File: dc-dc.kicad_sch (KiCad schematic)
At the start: 130 parts, among them SW3 CVS-02B, U30 NCP718ASN500T1G, U31 MPM54304GMN, U32 MPM54304GMN, U33 MAX16150AUT+T, U34 NCP451AFCT2G, U35 SN74LVC1G125DBVR, U36 LM3880, U37 MP8869S, U38 TPS7A20185PDQNR, U39 NCP51400MNTXG, U40 XC6230H001ER-G, U41 REF3012AIDBZT

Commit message: Finish connecting MCU
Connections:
- net SEQ_EN: now reaches C339.1, R308.1, U36.3 (EN)
- net ~{PB_CTRL_CLR} renamed SUP_MCU.SW_STATE
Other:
- note added: "NOTE2: when Res to GND mounted -> Alawys ON mount sequencer EN cap"
- note added: "NOTE: mount 1/2"
- note added: "NOTE: populate when Always ON (see NOTE2)"
- note added: "Todo: POE_DC signal is not connected Change 5V_AON to 3.3V_AON"
- note removed: "DNP for always ON"
- note removed: "Mount 1/2"
- note removed: "Mount only for Always-ON"
- note removed: "Todo: POE_DC signal is not connected"
- moved on the sheet: C336, C337, C339, D33, R283, R284, R293, R294, R308, U33, U35

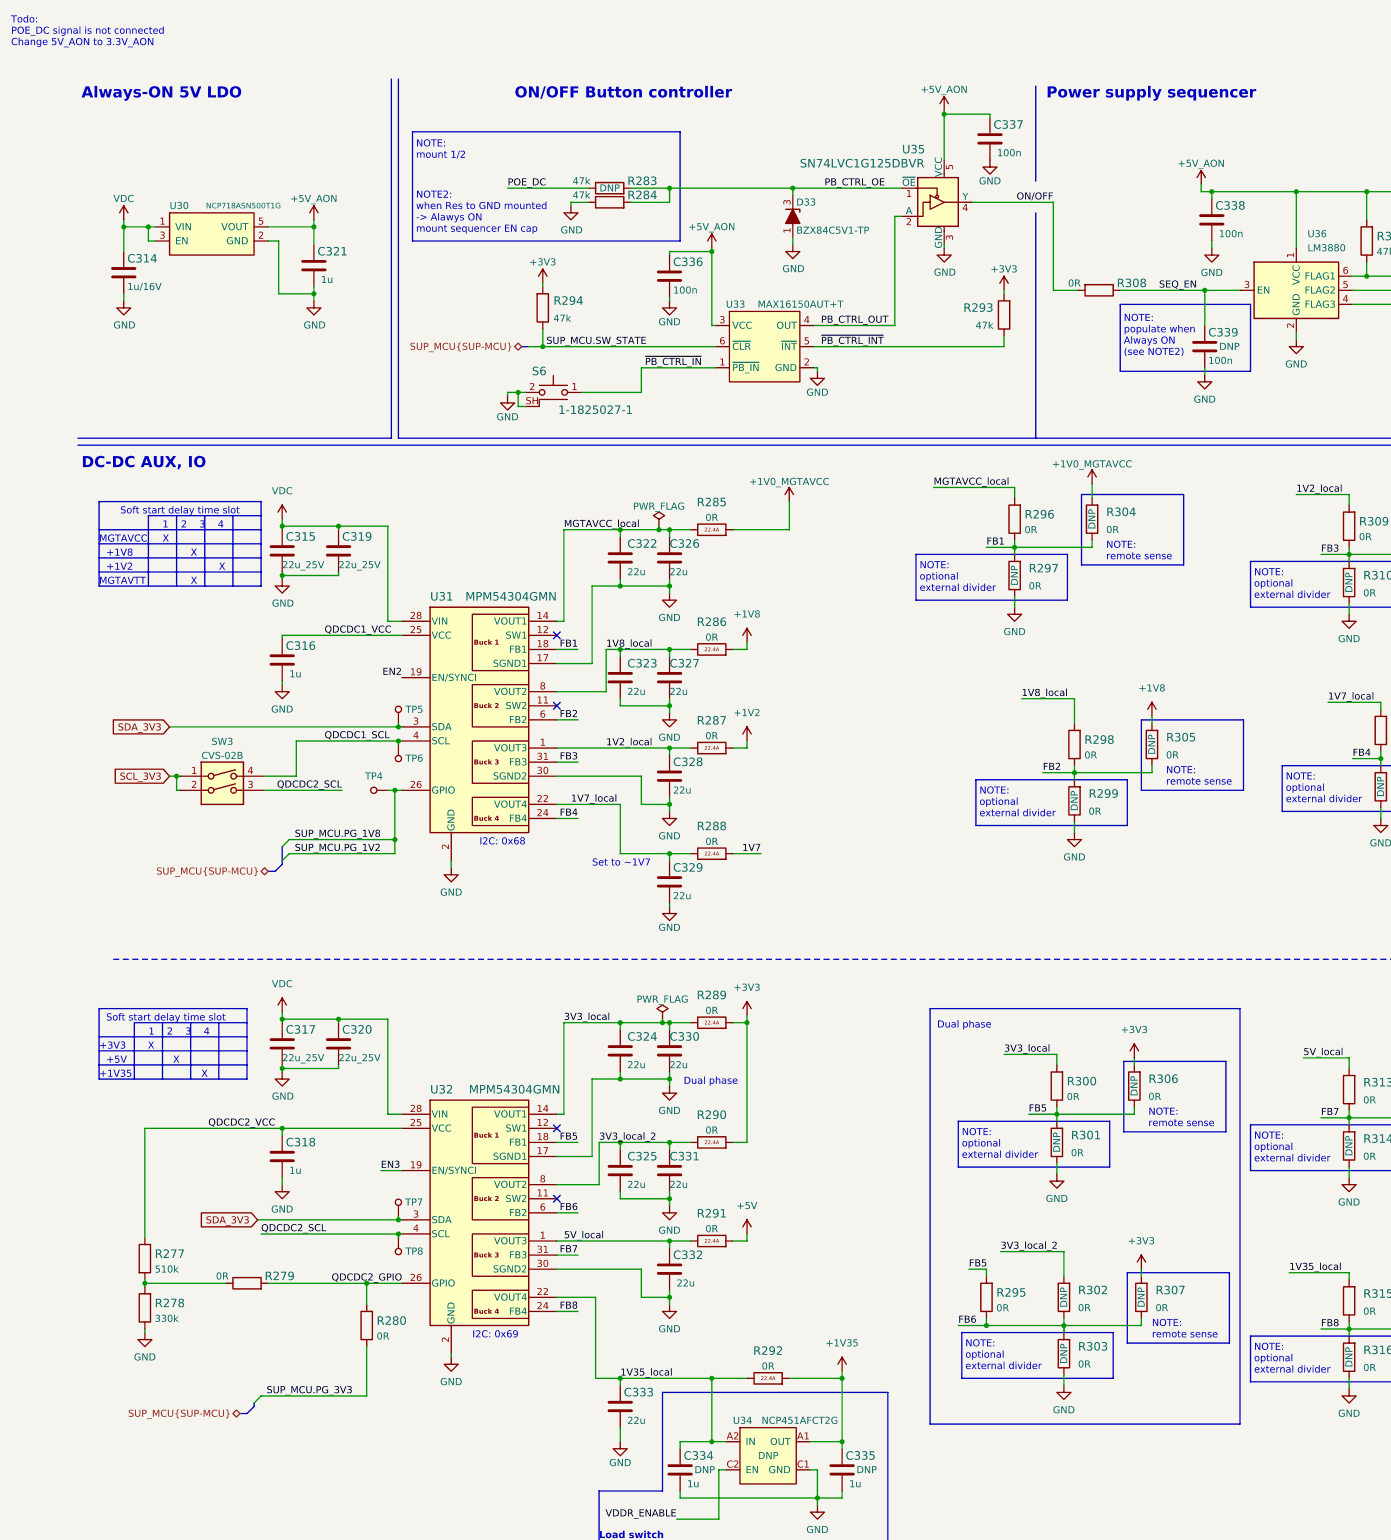
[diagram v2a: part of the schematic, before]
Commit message: DC-DC sheet grouping and placement on PCB
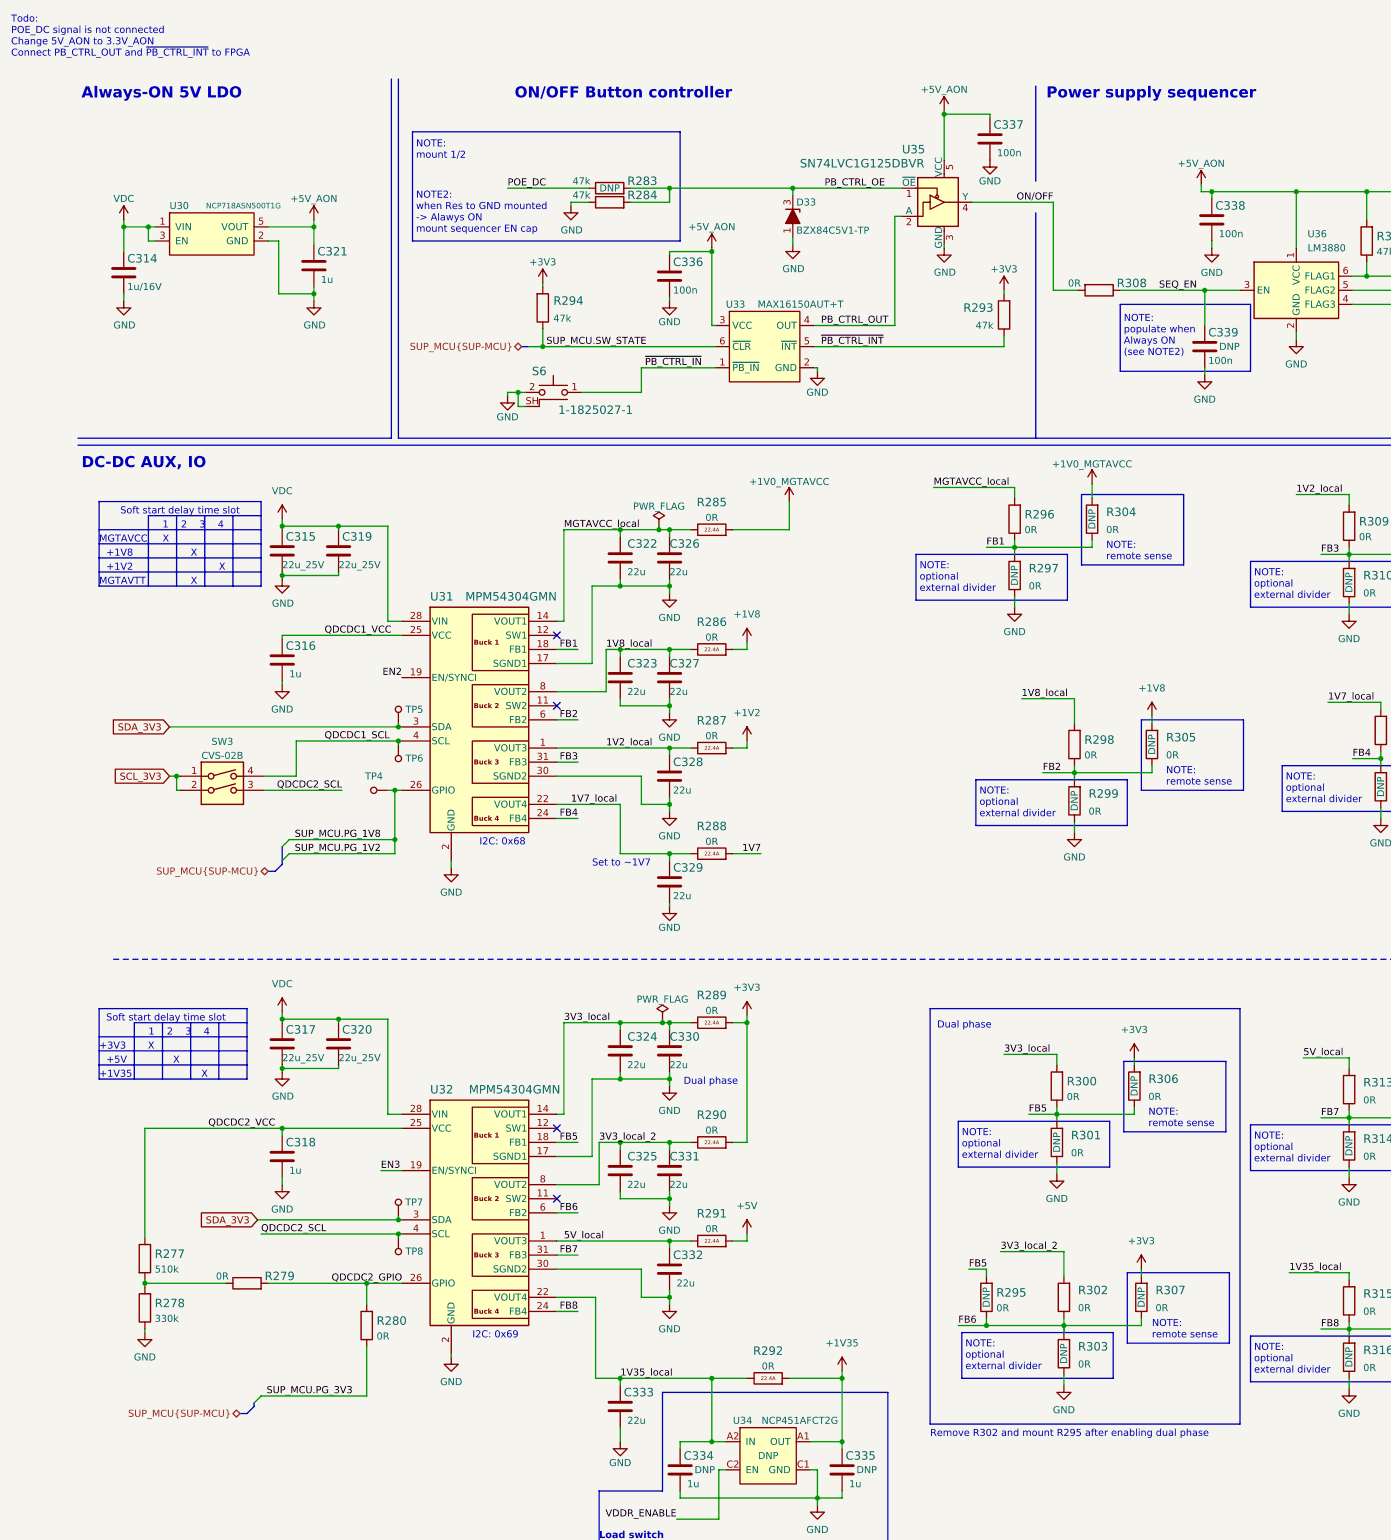
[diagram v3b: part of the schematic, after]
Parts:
- R295: DNP (none) -> DNP
- R302: DNP DNP -> (none)
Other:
- note added: "Remove R302 and mount R295 after enabling dual phase"
- note added: "Todo: POE_DC signal is not connected Change 5V_AON to 3.3V_AON Connect PB_CTRL_OUT and ~{PB_CTRL_INT} to FPGA"
- note removed: "Todo: POE_DC signal is not connected Change 5V_AON to 3.3V_AON"
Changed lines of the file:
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@@
     (effects (font (size 1.27 1.27)) (justify left bottom))
   )
-  (text "Todo:\nPOE_DC signal is not connected\nChange 5V_AON to 3.3V_AON"
-    (at 0.635 6.985 0)
+  (text "Todo:\nPOE_DC signal is not connected\nChange 5V_AON to 3.3V_AON\nConnect PB_CTRL_OUT and ~{PB_CTRL_INT} to FPGA"
+    (at 0.635 8.89 0)
     (effects (font (size 1.27 1.27)) (justify left bottom))
   )
@@
     (effects (font (size 2 2) (thickness 0.254) bold) (justify left bottom))
   )
+  (text "Remove R302 and mount R295 after enabling dual phase"
+    (at 166.37 257.81 0)
+    (effects (font (size 1.27 1.27)) (justify left bottom))
+  )
   (text "NOTE:\nmount 1/2" (at 73.66 27.305 0)
     (effects (font (size 1.27 1.27)) (justify left bottom))
@@
       (effects (font (size 1.27 1.27)) (justify right))
     )
-    (property "DNP" "DNP" (id 7) (at 190.5 232.41 0))
     (pin "1")
     (pin "2")
@@
   )
   (symbol (lib_id "antmicroResistors0402:R_0R_0402") (at 176.53 232.41 90) (unit 1)
-    (in_bom yes) (on_board yes) (fields_autoplaced)
+    (in_bom yes) (on_board yes)
     (property "Reference" "R295" (id 0) (at 178.308 231.5754 90)
       (effects (font (size 1.524 1.524)) (justify right))
@@
       (effects (font (size 1.27 1.27)) (justify right))
     )
+    (property "DNP" "DNP" (id 7) (at 176.53 232.41 0))
     (pin "1")
     (pin "2")

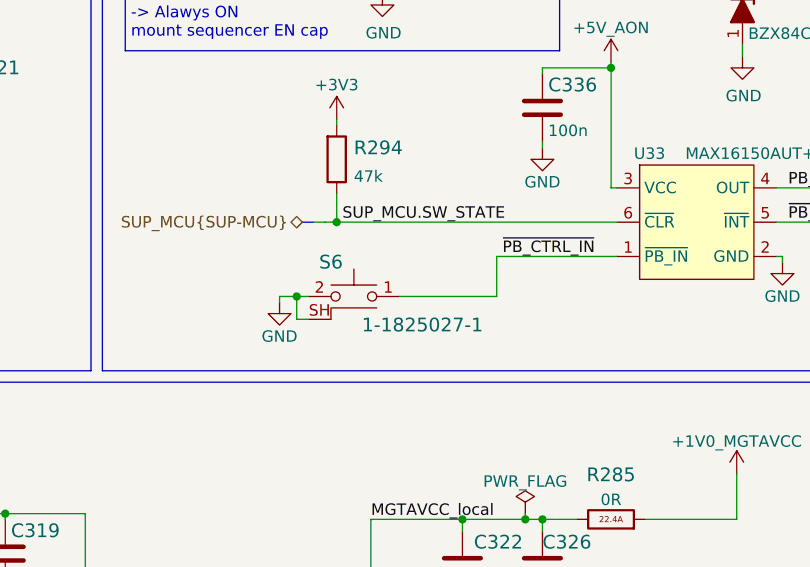
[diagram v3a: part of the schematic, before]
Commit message: Unify used buttons
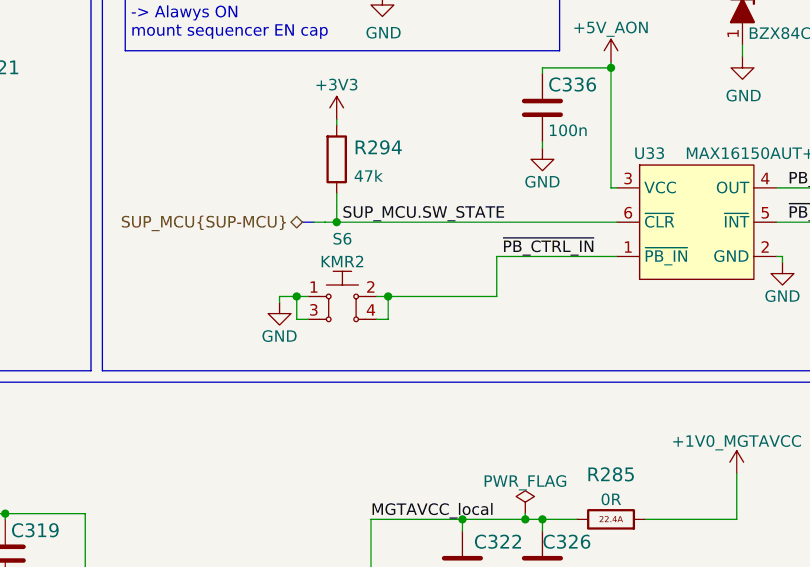
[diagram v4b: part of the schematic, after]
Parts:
- removed S6: 1-1825027-1, antmicro-footprints:TE_1-1825027-1, symbol antmicroTactileSwitches:1-1825027-1
- added S6: KMR2, antmicro-footprints:SW_SPST_4.2x2.8, symbol antmicroPushbuttonSwitches:KMR2
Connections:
- net GND: now also S6.1, S6.3
- net ~{PB_CTRL_IN}: now also S6.2, S6.4
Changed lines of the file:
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@@
   (junction (at 370.205 55.245) (diameter 0) (color 0 0 0 0)
   )
+  (junction (at 102.235 69.215) (diameter 0) (color 0 0 0 0)
+  )
   (junction (at 69.85 149.86) (diameter 0) (color 0 0 0 0)
   )
@@
     (stroke (width 0) (type default) (color 0 0 0 0))
   )
+  (wire (pts (xy 102.235 71.755) (xy 100.965 71.755))
+    (stroke (width 0) (type default) (color 0 0 0 0))
+  )
   (wire (pts (xy 192.405 137.795) (xy 206.375 137.795))
     (stroke (width 0) (type default) (color 0 0 0 0))
@@
     (stroke (width 0) (type default) (color 0 0 0 0))
   )
+  (wire (pts (xy 102.235 69.215) (xy 114.3 69.215))
+    (stroke (width 0) (type default) (color 0 0 0 0))
+  )
   (wire (pts (xy 379.095 45.085) (xy 379.095 46.355))
     (stroke (width 0) (type default) (color 0 0 0 0))
@@
     (stroke (width 0) (type default) (color 0 0 0 0))
   )
+  (wire (pts (xy 102.235 69.215) (xy 102.235 71.755))
+    (stroke (width 0) (type default) (color 0 0 0 0))
+  )
   (wire (pts (xy 206.375 127.635) (xy 206.375 128.905))
     (stroke (width 0) (type default) (color 0 0 0 0))
@@
     (stroke (width 0) (type default) (color 0 0 0 0))
   )
-  (wire (pts (xy 114.3 69.215) (xy 103.505 69.215))
+  (wire (pts (xy 100.965 69.215) (xy 102.235 69.215))
     (stroke (width 0) (type default) (color 0 0 0 0))
   )
@@
     (pin "2")
   )
+  (symbol (lib_id "antmicroPushbuttonSwitches:KMR2") (at 97.155 69.215 0) (unit 1)
+    (in_bom yes) (on_board yes) (fields_autoplaced)
+    (property "Reference" "S6" (id 0) (at 97.155 62.8482 0))
+    (property "Value" "KMR2" (id 1) (at 97.155 65.3851 0))
+    (property "Footprint" "antmicro-footprints:SW_SPST_4.2x2.8" (id 2) (at 102.235 64.135 0)
+      (effects (font (size 1.27 1.27)) (justify left) hide)
+    )
+    (property "Datasheet" "http://www.farnell.com/datasheets/2631211.pdf" (id 3) (at 102.235 61.595 0)
+      (effects (font (size 1.524 1.524)) (justify left) hide)
+    )
+    (property "MPN" "KMR211NGLFS" (id 4) (at 102.1334 59.2328 0)
+      (effects (font (size 1.524 1.524)) (justify left) hide)
+    )
+    (property "Manufacturer" "C&K Components" (id 5) (at 102.235 57.2262 0)
+      (effects (font (size 1.524 1.524)) (justify left) hide)
+    )
+    (pin "1")
+    (pin "2")
+    (pin "3")
+    (pin "4")
+  )
   (symbol (lib_id "antmicroCapacitors0402:C_10u_0402") (at 350.52 117.475 0) (unit 1)
     (in_bom yes) (on_board yes)
@@
     (pin "1")
   )
-  (symbol (lib_id "antmicroTactileSwitches:1-1825027-1") (at 98.425 67.945 0) (mirror y) (unit 1)
-    (in_bom yes) (on_board yes)
-    (property "Reference" "S6" (id 0) (at 95.885 65.405 0)
-      (effects (font (size 1.524 1.524)))
-    )
-    (property "Value" "1-1825027-1" (id 1) (at 106.045 72.39 0)
-      (effects (font (size 1.524 1.524)))
-    )
-    (property "Footprint" "antmicro-footprints:TE_1-1825027-1" (id 2) (at 93.345 62.865 0)
-      (effects (font (size 1.524 1.524)) (justify left) hide)
-    )
-    (property "Datasheet" "https://www.te.com/commerce/DocumentDelivery/DDEController?Action=showdoc&DocId=Customer+Drawing%7F1825027%7FH1%7Fpdf%7FEnglish%7FENG_CD_1825027_H1.pdf%7F1-1825027-1" (id 3) (at 93.345 60.325 0)
-      (effects (font (size 1.524 1.524)) (justify left) hide)
-    )
-    (property "MPN" "1-1825027-1" (id 4) (at 93.345 55.245 0)
-      (effects (font (size 1.524 1.524)) (justify left) hide)
-    )
-    (property "Manufacturer" "TE Connectivity" (id 5) (at 93.345 40.005 0)
-      (effects (font (size 1.524 1.524)) (justify left) hide)
-    )
-    (pin "1")
-    (pin "2")
-    (pin "SH")
-  )
   (symbol (lib_id "antmicroResistors0402:R_0R_0402") (at 189.23 194.31 90) (unit 1)

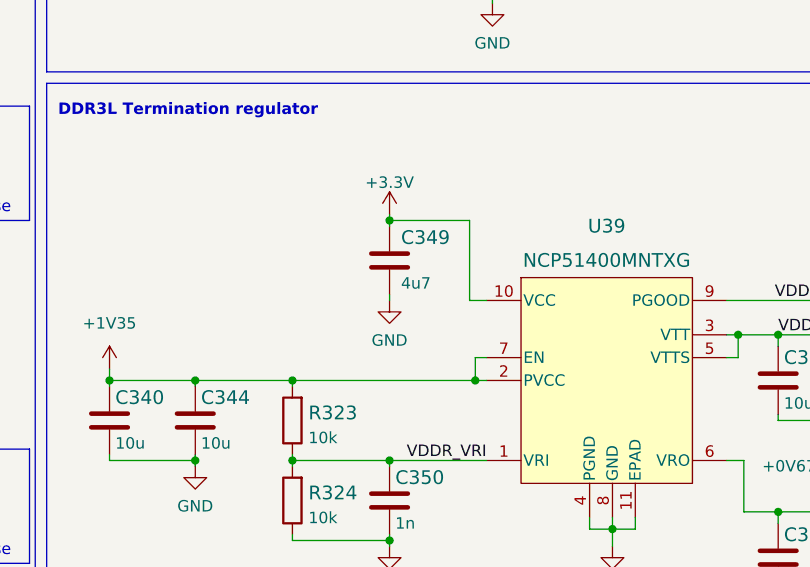
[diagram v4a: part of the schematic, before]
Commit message: Increase 0201 to 0402 components where possible (EIA 0402 footprint)
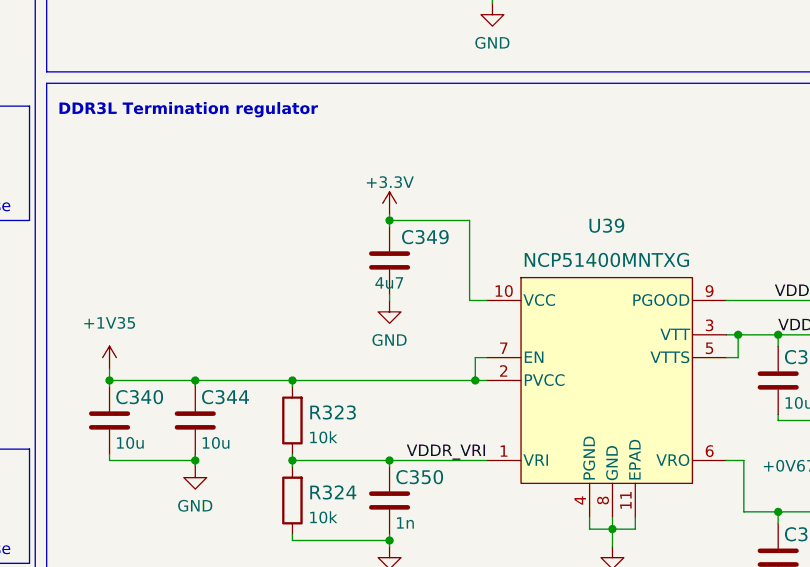
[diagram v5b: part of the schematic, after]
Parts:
- C349: value C_4u7_0402 -> C_4u7_0402_EIA; footprint antmicro-footprints:0402-cap -> antmicro-footprints:0201-cap; symbol antmicroCapacitors0402:C_4u7_0402 -> antmicroCapacitorsmisc:C_4u7_0201; MPN GRM155R61A475MEAAD -> GRM035R60J475ME15D; Manufacturer MURATA -> Murata
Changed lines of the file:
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@@
     (pin "1")
   )
-  (symbol (lib_id "antmicroCapacitors0402:C_4u7_0402") (at 312.42 207.645 0) (unit 1)
+  (symbol (lib_id "antmicroCapacitorsmisc:C_4u7_0201") (at 312.42 207.645 0) (unit 1)
     (in_bom yes) (on_board yes)
     (property "Reference" "C349" (id 0) (at 313.69 205.105 0)
       (effects (font (size 1.524 1.524)) (justify left))
     )
-    (property "Value" "C_4u7_0402" (id 1) (at 312.42 211.455 0)
+    (property "Value" "C_4u7_0402_EIA" (id 1) (at 312.42 211.455 0)
       (effects (font (size 1.524 1.524)) hide)
     )
-    (property "Footprint" "antmicro-footprints:0402-cap" (id 2) (at 317.5 202.565 0)
+    (property "Footprint" "antmicro-footprints:0201-cap" (id 2) (at 317.5 202.565 0)
       (effects (font (size 1.524 1.524)) (justify left) hide)
     )
@@
       (effects (font (size 1.27 1.27)) hide)
     )
-    (property "Manufacturer" "MURATA" (id 4) (at 317.5 197.485 0)
+    (property "Manufacturer" "Murata" (id 4) (at 317.5 197.485 0)
       (effects (font (size 1.524 1.524)) (justify left) hide)
     )
-    (property "MPN" "GRM155R61A475MEAAD" (id 5) (at 317.5 200.025 0)
+    (property "MPN" "GRM035R60J475ME15D" (id 5) (at 317.5 200.025 0)
       (effects (font (size 1.524 1.524)) (justify left) hide)
     )
-    (property "Val" "4u7" (id 6) (at 313.69 210.185 0)
-      (effects (font (size 1.27 1.27)) (justify left))
-    )
+    (property "Val" "4u7" (id 6) (at 312.42 210.185 0))
     (pin "1")
     (pin "2")
